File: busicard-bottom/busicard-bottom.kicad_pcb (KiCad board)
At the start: 2 copper layers, 70 x 46 mm, 18 parts, among them SW1 SW_Push, U1 ZXSC380FHTA

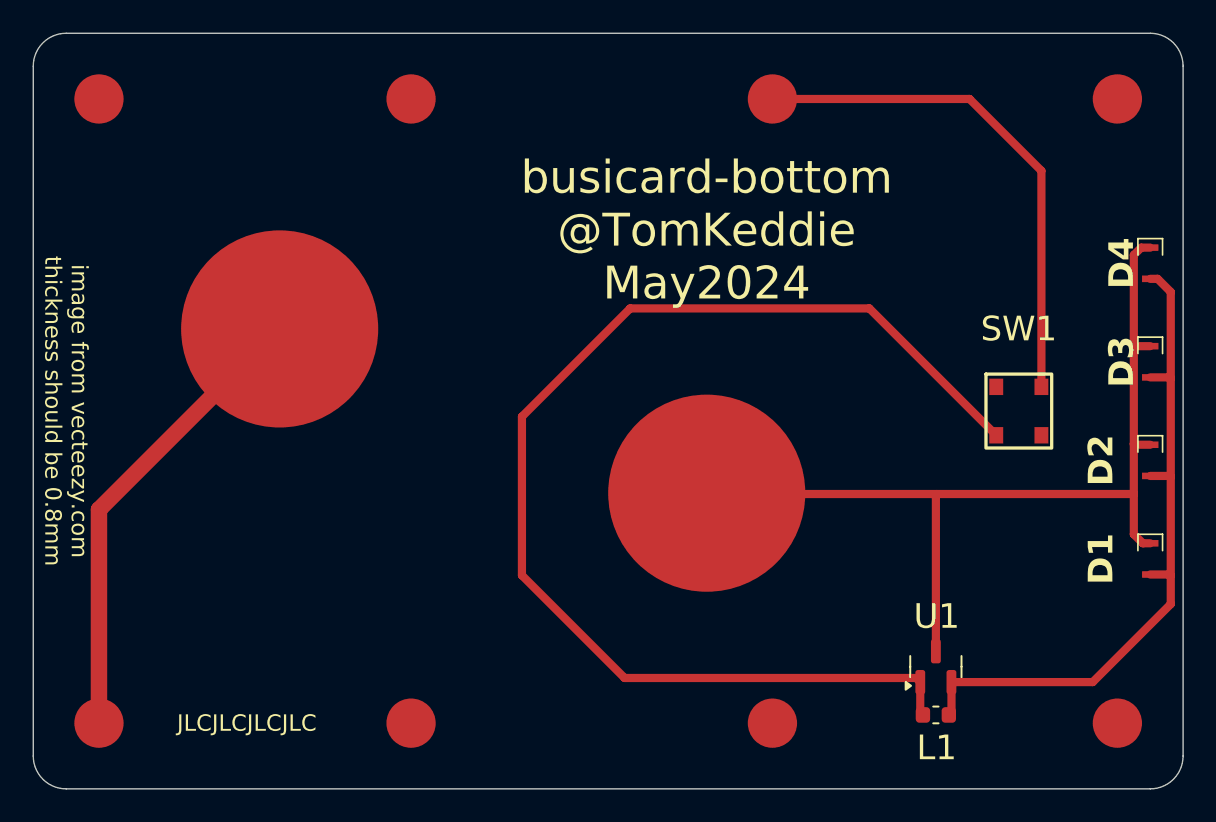
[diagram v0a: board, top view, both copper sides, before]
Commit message: busicard-bottom: fix bom and cpl inc rotation
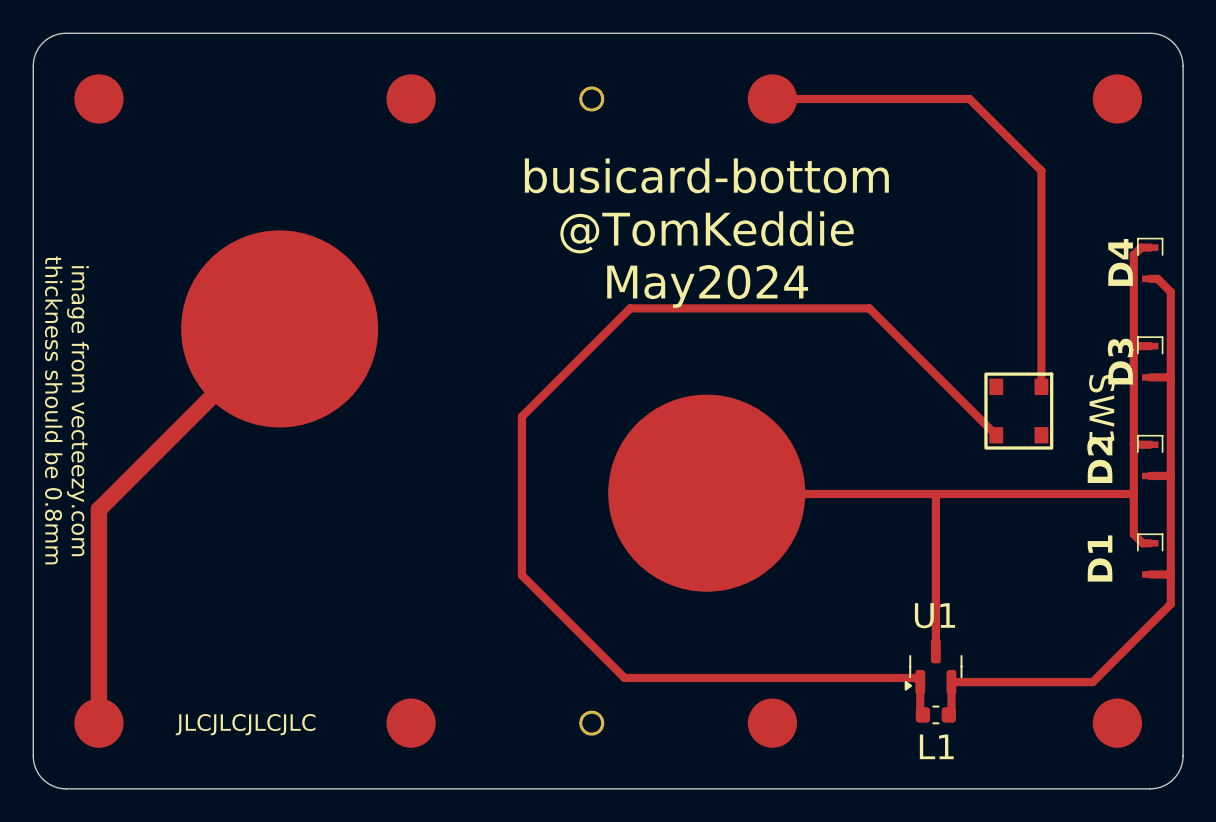
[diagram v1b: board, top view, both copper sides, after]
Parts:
- added H1: mech-only-no-pins, lib:JLC_ASSEMBLY_HOLE, F.Cu at (164.0, 81.0)
- added H2: mech-only-no-pins, lib:JLC_ASSEMBLY_HOLE, F.Cu at (164.0, 119.0)
- turned SW1 to -90 degrees
- turned U1 to -90 degrees

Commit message: busicard-top: enlarge battery opening
move all mount points 0.5mm towards edges
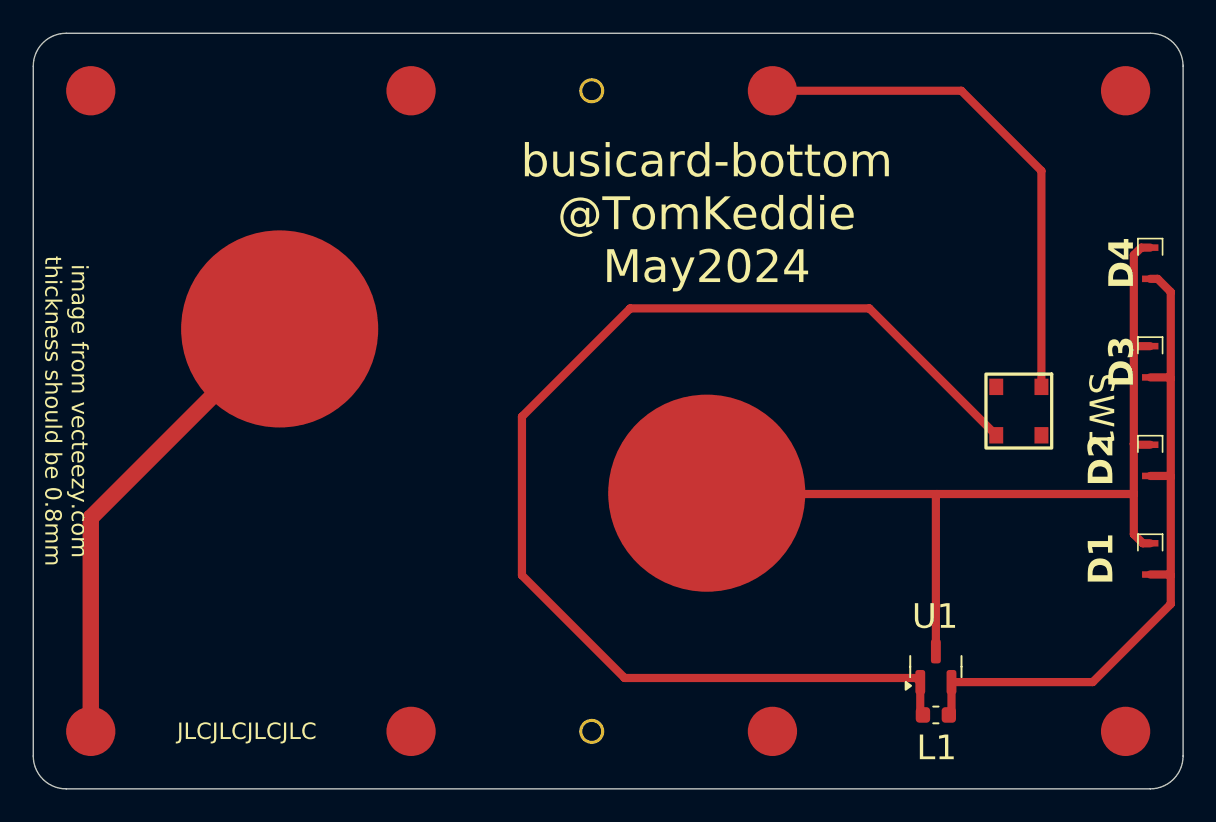
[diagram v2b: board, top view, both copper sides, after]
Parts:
- moved TP10 0.71 mm to (133.5, 80.5)
- moved TP4 0.71 mm to (133.5, 119.5)
- moved TP5 0.71 mm to (196.5, 119.5)
- moved TP6 0.71 mm to (196.5, 80.5)
- moved H1 0.50 mm to (164.0, 80.5)
- moved H2 0.50 mm to (164.0, 119.5)
- moved TP1 0.50 mm to (175.0, 80.5)
- moved TP7 0.50 mm to (153.0, 119.5)
- moved TP8 0.50 mm to (153.0, 80.5)
- moved TP9 0.50 mm to (175.0, 119.5)
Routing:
- net /BATT1-: track 28.6 -> 29.3 mm
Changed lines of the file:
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@@
 	(footprint "lib:interconnect-base"
 		(layer "F.Cu")
-		(at 175 119)
+		(at 175 119.5)
 		(property "Reference" "TP9"
 			(at 0 -2.25 0)
@@
 	(footprint "lib:interconnect-base"
 		(layer "F.Cu")
-		(at 175 81)
+		(at 175 80.5)
 		(property "Reference" "TP1"
 			(at 0 -2.25 0)
@@
 	(footprint "lib:interconnect-base"
 		(layer "F.Cu")
-		(at 134 81)
+		(at 133.5 80.5)
 		(property "Reference" "TP10"
 			(at 0 -2.25 0)
@@
 	(footprint "lib:interconnect-base"
 		(layer "F.Cu")
-		(at 196 119)
+		(at 196.5 119.5)
 		(property "Reference" "TP5"
 			(at 0 -2.25 0)
@@
 	(footprint "lib:JLC_ASSEMBLY_HOLE"
 		(layer "F.Cu")
-		(at 164 81)
+		(at 164 80.5)
 		(property "Reference" "H1"
 			(at 0 -1.5 0)
@@
 	(footprint "lib:interconnect-base"
 		(layer "F.Cu")
-		(at 196 81)
+		(at 196.5 80.5)
 		(property "Reference" "TP6"
 			(at 0 -2.25 0)
@@
 	(footprint "lib:interconnect-base"
 		(layer "F.Cu")
-		(at 153 81)
+		(at 153 80.5)
 		(property "Reference" "TP8"
 			(at 0 -2.25 0)
@@
 	(footprint "lib:interconnect-base"
 		(layer "F.Cu")
-		(at 134 119)
+		(at 133.5 119.5)
 		(property "Reference" "TP4"
 			(at 0 -2.25 0)
@@
 	(footprint "lib:interconnect-base"
 		(layer "F.Cu")
-		(at 153 119)
+		(at 153 119.5)
 		(property "Reference" "TP7"
 			(at 0 -2.25 0)
@@
 	(footprint "lib:JLC_ASSEMBLY_HOLE"
 		(layer "F.Cu")
-		(at 164 119)
+		(at 164 119.5)
 		(property "Reference" "H2"
 			(at 0 -1.5 0)
@@
 		(fp_poly
 			(pts
-				(xy -4.533258 0.021923) (xy -4.239059 0.016993) (xy -4.004719 0.007918) (xy -3.820638 -0.006092)
+				(xy -4.533259 0.021923) (xy -4.239059 0.016993) (xy -4.004719 0.007918) (xy -3.820638 -0.006092)
 				(xy -3.677217 -0.025825) (xy -3.564855 -0.052072) (xy -3.473956 -0.085621) (xy -3.394918 -0.127262)
 				(xy -3.318144 -0.177783) (xy -3.298349 -0.191772) (xy -3.153214 -0.341507) (xy -3.02556 -0.556742)
@@
 				(xy -13.375499 -0.045969) (xy -13.207317 -0.038742) (xy -12.960194 -0.031718) (xy -12.643789 -0.025066)
 				(xy -12.267759 -0.018952) (xy -11.841765 -0.013542) (xy -11.375465 -0.009003) (xy -10.878517 -0.005502)
-				(xy -10.611993 -0.004151) (xy -10.017189 -0.001472) (xy -9.378273 0.001523) (xy -8.716156 0.004727)
+				(xy -10.611993 -0.004151) (xy -10.017189 -0.001472) (xy -9.378273 0.001523) (xy -8.716157 0.004727)
 				(xy -8.051746 0.008036) (xy -7.405955 0.011344) (xy -6.799692 0.014546) (xy -6.253868 0.017537)
 				(xy -5.870987 0.019729) (xy -5.339621 0.022502) (xy -4.896911 0.023496)
@@
 				(xy -32.478838 0.825061) (xy -32.484119 1.891489) (xy -32.486466 2.469681) (xy -32.486932 2.958036)
 				(xy -32.484974 3.364967) (xy -32.480049 3.698886) (xy -32.471613 3.968208) (xy -32.459123 4.181344)
-				(xy -32.442034 4.346708) (xy -32.419805 4.472712) (xy -32.391891 4.567771) (xy -32.357748 4.640296)
+				(xy -32.442034 4.346708) (xy -32.419805 4.472712) (xy -32.391891 4.567771) (xy -32.357747 4.640296)
 				(xy -32.316836 4.698701) (xy -32.301639 4.716441) (xy -32.251434 4.790399) (xy -32.244797 4.82079)
 				(xy -32.221199 4.884711) (xy -32.142589 4.995561) (xy -32.026457 5.133951) (xy -31.890293 5.280489)
@@
 				(xy 32.514689 -0.762389) (xy 32.522681 -1.356827) (xy 32.529045 -1.965424) (xy 32.53373 -2.57713)
 				(xy 32.536685 -3.180896) (xy 32.537857 -3.765674) (xy 32.537197 -4.320414) (xy 32.534651 -4.834068)
-				(xy 32.53017 -5.295587) (xy 32.523701 -5.693922) (xy 32.515194 -6.018022) (xy 32.504596 -6.256843)
+				(xy 32.53017 -5.295587) (xy 32.523701 -5.693922) (xy 32.515194 -6.018021) (xy 32.504596 -6.256843)
 				(xy 32.502554 -6.288588) (xy 32.491546 -6.465577) (xy 32.477958 -6.708125) (xy 32.463552 -6.983628)
 				(xy 32.450698 -7.246616) (xy 32.437581 -7.502638) (xy 32.423602 -7.736714) (xy 32.410374 -7.92404)
@@
 				(xy 7.035548 5.895402) (xy 7.039206 5.731801) (xy 7.042937 5.485136) (xy 7.046717 5.162097) (xy 7.050519 4.769379)
 				(xy 7.05432 4.313673) (xy 7.058096 3.801673) (xy 7.06182 3.240069) (xy 7.065469 2.635555) (xy 7.069018 1.994824)
-				(xy 7.072442 1.324567) (xy 7.075716 0.631478) (xy 7.078815 -0.077752) (xy 7.081716 -0.796429) (xy 7.084392 -1.517861)
+				(xy 7.072442 1.324567) (xy 7.075716 0.631478) (xy 7.078815 -0.077752) (xy 7.081716 -0.796429) (xy 7.084392 -1.51786)
 				(xy 7.08682 -2.235358) (xy 7.088975 -2.942224) (xy 7.090832 -3.631769) (xy 7.092366 -4.297299) (xy 7.093552 -4.932122)
 				(xy 7.094366 -5.529545) (xy 7.094783 -6.082877) (xy 7.094778 -6.585424) (xy 7.094327 -7.030495)
@@
 	)
 	(gr_text "JLCJLCJLCJLC"
-		(at 143 119 0)
+		(at 143 119.5 0)
 		(layer "F.SilkS")
 		(effects
@@
 	)
 	(gr_text "busicard-bottom\n@TomKeddie\nMay2024"
-		(at 171 89 0)
+		(at 171 88 0)
 		(layer "F.SilkS")
 		(effects
@@
 	)
 	(segment
-		(start 187 81)
+		(start 191.375 98.525)
 		(end 191.375 85.375)
 		(width 0.5)
@@
 	(segment
 		(start 191.375 85.375)
-		(end 191.375 98.525)
+		(end 186.5 80.5)
 		(width 0.5)
 		(layer "F.Cu")
@@
 	)
 	(segment
-		(start 175 81)
-		(end 187 81)
+		(start 186.5 80.5)
+		(end 175 80.5)
 		(width 0.5)
 		(layer "F.Cu")
 		(net 2)
+	)
+	(segment
+		(start 133.5 106.5)
+		(end 133.5 119.5)
+		(width 1)
+		(layer "F.Cu")
+		(net 5)
 	)
 	(segment
 		(start 145 95)
-		(end 134 106)
+		(end 133.5 106.5)
 		(width 1)
 		(layer "F.Cu")
-		(net 5)
-	)
-	(segment
-		(start 134 106)
-		(end 134 119)
-		(width 1)
-		(layer "F.Cu")
